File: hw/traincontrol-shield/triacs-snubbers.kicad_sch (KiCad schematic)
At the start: 6 parts, among them Q1 BT134W-600D, Q2 BT134W-600D

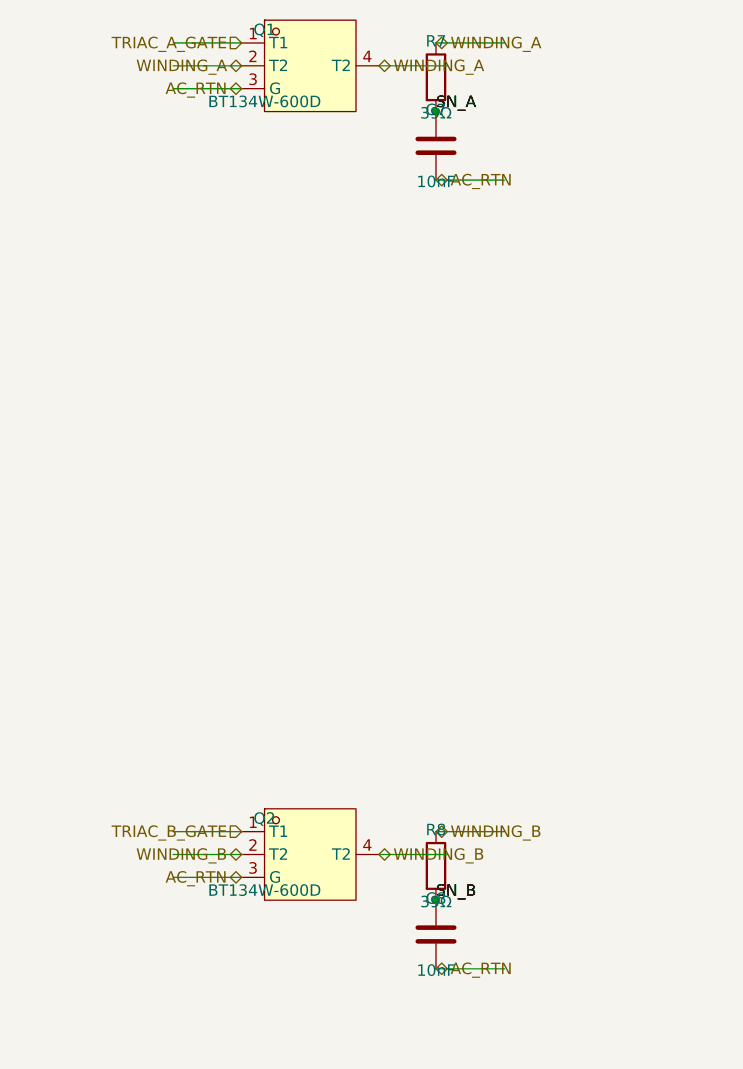
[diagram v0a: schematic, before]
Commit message: Fix hlabel placement: label sits at stub outer end (lx), not pin tip (x)
The hierarchical label connection point must be at lx (the outer end of
the stub wire), not at x (the IC pin tip). With the label at x, it was
overlapping the pin itself instead of sitting at the end of the routing
stub where it belongs.

  angle=180 (left-side): lx = x - STUB  → label to the left of pin ✓
  angle=0   (right-side): lx = x + STUB  → label to the right of pin ✓

Wire still runs x↔lx, connecting the IC pin to the label connection.
Updated gen_all_sheets.py and gen_power_supply.py.

Co-Authored-By: Claude Sonnet 4.6 <noreply@anthropic.com>
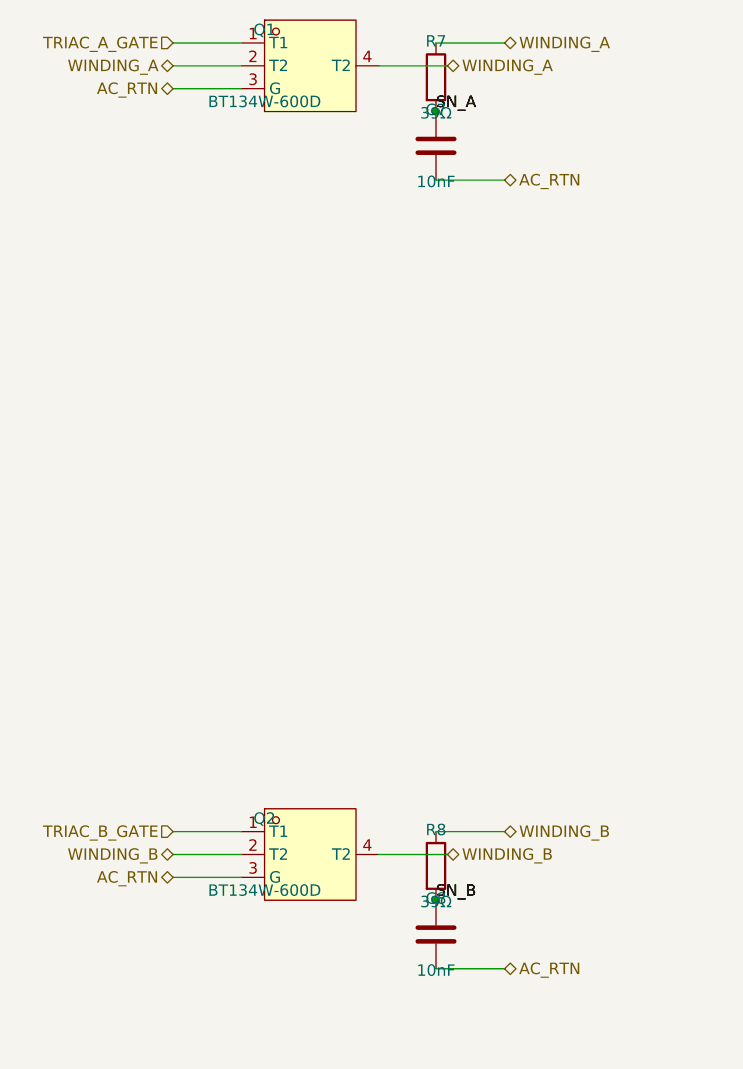
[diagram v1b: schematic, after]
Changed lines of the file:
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@@
 	(hierarchical_label "AC_RTN"
 		(shape bidirectional)
-		(at 77.47 92.71000000000001 180)
-		(fields_autoplaced yes)
-		(effects (font (size 1.27 1.27)) (justify right bottom))
-		(property "Intersheetrefs" "${INTERSHEET_REFS}"
-			(at 77.47 92.71000000000001 0)
+		(at 69.85 92.71000000000001 180)
+		(fields_autoplaced yes)
+		(effects (font (size 1.27 1.27)) (justify right bottom))
+		(property "Intersheetrefs" "${INTERSHEET_REFS}"
+			(at 69.85 92.71000000000001 0)
 			(effects (font (size 1.27 1.27)) (hide yes))
 		)
@@
 	(hierarchical_label "WINDING_A"
 		(shape bidirectional)
-		(at 77.47 90.17 180)
-		(fields_autoplaced yes)
-		(effects (font (size 1.27 1.27)) (justify right bottom))
-		(property "Intersheetrefs" "${INTERSHEET_REFS}"
-			(at 77.47 90.17 0)
+		(at 69.85 90.17 180)
+		(fields_autoplaced yes)
+		(effects (font (size 1.27 1.27)) (justify right bottom))
+		(property "Intersheetrefs" "${INTERSHEET_REFS}"
+			(at 69.85 90.17 0)
 			(effects (font (size 1.27 1.27)) (hide yes))
 		)
@@
 	(hierarchical_label "WINDING_A"
 		(shape bidirectional)
-		(at 92.71000000000001 90.17 0)
-		(fields_autoplaced yes)
-		(effects (font (size 1.27 1.27)) (justify left bottom))
-		(property "Intersheetrefs" "${INTERSHEET_REFS}"
-			(at 92.71000000000001 90.17 0)
+		(at 100.33000000000001 90.17 0)
+		(fields_autoplaced yes)
+		(effects (font (size 1.27 1.27)) (justify left bottom))
+		(property "Intersheetrefs" "${INTERSHEET_REFS}"
+			(at 100.33000000000001 90.17 0)
 			(effects (font (size 1.27 1.27)) (hide yes))
 		)
@@
 	(hierarchical_label "TRIAC_A_GATE"
 		(shape input)
-		(at 77.47 87.63 180)
-		(fields_autoplaced yes)
-		(effects (font (size 1.27 1.27)) (justify right bottom))
-		(property "Intersheetrefs" "${INTERSHEET_REFS}"
-			(at 77.47 87.63 0)
+		(at 69.85 87.63 180)
+		(fields_autoplaced yes)
+		(effects (font (size 1.27 1.27)) (justify right bottom))
+		(property "Intersheetrefs" "${INTERSHEET_REFS}"
+			(at 69.85 87.63 0)
 			(effects (font (size 1.27 1.27)) (hide yes))
 		)
@@
 	(hierarchical_label "WINDING_A"
 		(shape bidirectional)
-		(at 99.06 87.63 0)
-		(fields_autoplaced yes)
-		(effects (font (size 1.27 1.27)) (justify left bottom))
-		(property "Intersheetrefs" "${INTERSHEET_REFS}"
-			(at 99.06 87.63 0)
+		(at 106.68 87.63 0)
+		(fields_autoplaced yes)
+		(effects (font (size 1.27 1.27)) (justify left bottom))
+		(property "Intersheetrefs" "${INTERSHEET_REFS}"
+			(at 106.68 87.63 0)
 			(effects (font (size 1.27 1.27)) (hide yes))
 		)
@@
 	(hierarchical_label "AC_RTN"
 		(shape bidirectional)
-		(at 99.06 102.87 0)
-		(fields_autoplaced yes)
-		(effects (font (size 1.27 1.27)) (justify left bottom))
-		(property "Intersheetrefs" "${INTERSHEET_REFS}"
-			(at 99.06 102.87 0)
+		(at 106.68 102.87 0)
+		(fields_autoplaced yes)
+		(effects (font (size 1.27 1.27)) (justify left bottom))
+		(property "Intersheetrefs" "${INTERSHEET_REFS}"
+			(at 106.68 102.87 0)
 			(effects (font (size 1.27 1.27)) (hide yes))
 		)
@@
 	(hierarchical_label "AC_RTN"
 		(shape bidirectional)
-		(at 77.47 180.34 180)
-		(fields_autoplaced yes)
-		(effects (font (size 1.27 1.27)) (justify right bottom))
-		(property "Intersheetrefs" "${INTERSHEET_REFS}"
-			(at 77.47 180.34 0)
+		(at 69.85 180.34 180)
+		(fields_autoplaced yes)
+		(effects (font (size 1.27 1.27)) (justify right bottom))
+		(property "Intersheetrefs" "${INTERSHEET_REFS}"
+			(at 69.85 180.34 0)
 			(effects (font (size 1.27 1.27)) (hide yes))
 		)
@@
 	(hierarchical_label "WINDING_B"
 		(shape bidirectional)
-		(at 77.47 177.8 180)
-		(fields_autoplaced yes)
-		(effects (font (size 1.27 1.27)) (justify right bottom))
-		(property "Intersheetrefs" "${INTERSHEET_REFS}"
-			(at 77.47 177.8 0)
+		(at 69.85 177.8 180)
+		(fields_autoplaced yes)
+		(effects (font (size 1.27 1.27)) (justify right bottom))
+		(property "Intersheetrefs" "${INTERSHEET_REFS}"
+			(at 69.85 177.8 0)
 			(effects (font (size 1.27 1.27)) (hide yes))
 		)
@@
 	(hierarchical_label "WINDING_B"
 		(shape bidirectional)
-		(at 92.71000000000001 177.8 0)
-		(fields_autoplaced yes)
-		(effects (font (size 1.27 1.27)) (justify left bottom))
-		(property "Intersheetrefs" "${INTERSHEET_REFS}"
-			(at 92.71000000000001 177.8 0)
+		(at 100.33000000000001 177.8 0)
+		(fields_autoplaced yes)
+		(effects (font (size 1.27 1.27)) (justify left bottom))
+		(property "Intersheetrefs" "${INTERSHEET_REFS}"
+			(at 100.33000000000001 177.8 0)
 			(effects (font (size 1.27 1.27)) (hide yes))
 		)
@@
 	(hierarchical_label "TRIAC_B_GATE"
 		(shape input)
-		(at 77.47 175.26000000000002 180)
-		(fields_autoplaced yes)
-		(effects (font (size 1.27 1.27)) (justify right bottom))
-		(property "Intersheetrefs" "${INTERSHEET_REFS}"
-			(at 77.47 175.26000000000002 0)
+		(at 69.85 175.26000000000002 180)
+		(fields_autoplaced yes)
+		(effects (font (size 1.27 1.27)) (justify right bottom))
+		(property "Intersheetrefs" "${INTERSHEET_REFS}"
+			(at 69.85 175.26000000000002 0)
 			(effects (font (size 1.27 1.27)) (hide yes))
 		)
@@
 	(hierarchical_label "WINDING_B"
 		(shape bidirectional)
-		(at 99.06 175.26000000000002 0)
-		(fields_autoplaced yes)
-		(effects (font (size 1.27 1.27)) (justify left bottom))
-		(property "Intersheetrefs" "${INTERSHEET_REFS}"
-			(at 99.06 175.26000000000002 0)
+		(at 106.68 175.26000000000002 0)
+		(fields_autoplaced yes)
+		(effects (font (size 1.27 1.27)) (justify left bottom))
+		(property "Intersheetrefs" "${INTERSHEET_REFS}"
+			(at 106.68 175.26000000000002 0)
 			(effects (font (size 1.27 1.27)) (hide yes))
 		)
@@
 	(hierarchical_label "AC_RTN"
 		(shape bidirectional)
-		(at 99.06 190.50000000000003 0)
-		(fields_autoplaced yes)
-		(effects (font (size 1.27 1.27)) (justify left bottom))
-		(property "Intersheetrefs" "${INTERSHEET_REFS}"
-			(at 99.06 190.50000000000003 0)
-			(effects (font (size 1.27 1.27)) (hide yes))
-		)
+		(at 106.68 190.50000000000003 0)
+		(fields_autoplaced yes)
+		(effects (font (size 1.27 1.27)) (justify left bottom))
+		(property "Intersheetrefs" "${INTERSHEET_REFS}"
+			(at 106.68 190.50000000000003 0)
+			(effects (font (size 1.27 1.27)) (hide yes))
+		)

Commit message: Add wire stub to net_label, matching hlabel placement convention
net_label() now generates a short wire stub (length STUB) between the
component pin tip (x) and the label connection point (lx), placing the
label at the outer end of the stub — identical to how hlabel works:

  angle=180 (left-side):  lx = x - STUB, label left of pin  ✓
  angle=0   (right-side): lx = x + STUB, label right of pin ✓

Also fix XOR_OUT net labels at U4A/B left-side input pins (angle=0→180)
so their stubs extend leftward away from the IC body.

Updated gen_all_sheets.py and gen_power_supply.py.

Co-Authored-By: Claude Sonnet 4.6 <noreply@anthropic.com>
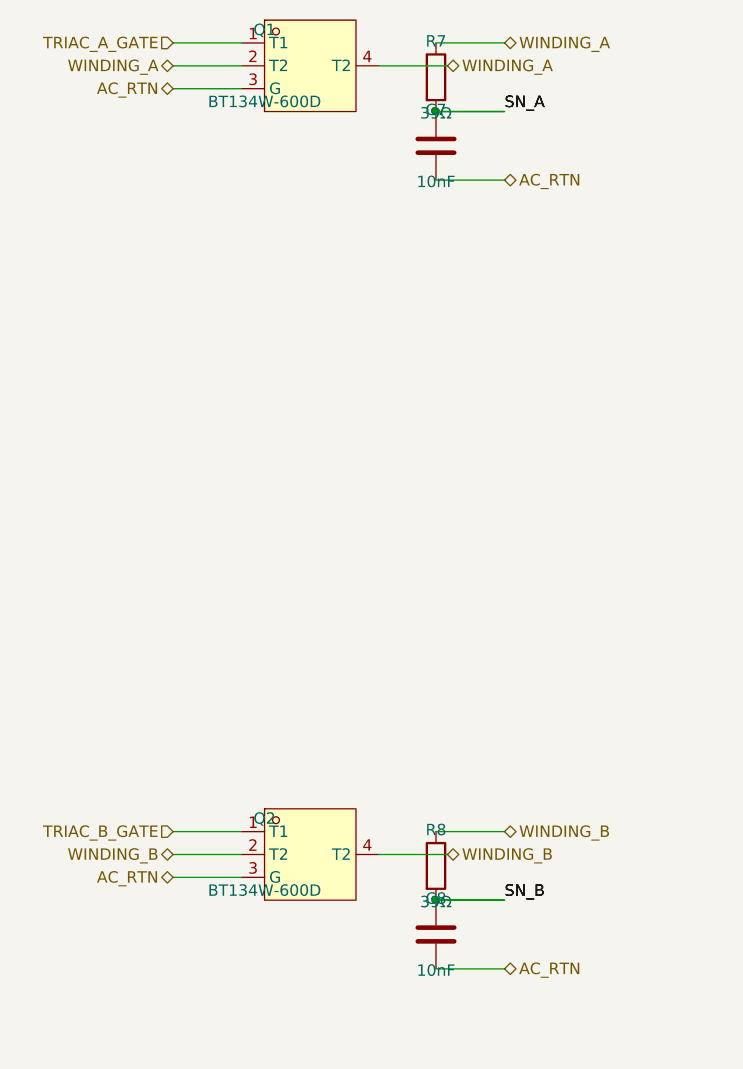
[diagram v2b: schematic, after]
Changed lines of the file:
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@@
 		)
+	)
+	(wire
+		(pts (xy 99.06 95.25) (xy 106.68 95.25))
+		(stroke (width 0) (type solid))
 	)
 	(label "SN_A"
-		(at 99.06 95.25 0)
+		(at 106.68 95.25 0)
 		(fields_autoplaced yes)
 		(effects (font (size 1.27 1.27)) (justify left bottom))
@@
 		)
 	)
+	(wire
+		(pts (xy 99.06 95.25) (xy 106.68 95.25))
+		(stroke (width 0) (type solid))
+	)
 	(label "SN_A"
-		(at 99.06 95.25 0)
+		(at 106.68 95.25 0)
 		(fields_autoplaced yes)
 		(effects (font (size 1.27 1.27)) (justify left bottom))
@@
 		)
 	)
+	(wire
+		(pts (xy 99.06 182.88000000000002) (xy 106.68 182.88000000000002))
+		(stroke (width 0) (type solid))
+	)
 	(label "SN_B"
-		(at 99.06 182.88000000000002 0)
+		(at 106.68 182.88000000000002 0)
 		(fields_autoplaced yes)
 		(effects (font (size 1.27 1.27)) (justify left bottom))
@@
 		)
 	)
+	(wire
+		(pts (xy 99.06 182.88000000000002) (xy 106.68 182.88000000000002))
+		(stroke (width 0) (type solid))
+	)
 	(label "SN_B"
-		(at 99.06 182.88000000000002 0)
-		(fields_autoplaced yes)
-		(effects (font (size 1.27 1.27)) (justify left bottom))
+		(at 106.68 182.88000000000002 0)
+		(fields_autoplaced yes)
+		(effects (font (size 1.27 1.27)) (justify left bottom))
